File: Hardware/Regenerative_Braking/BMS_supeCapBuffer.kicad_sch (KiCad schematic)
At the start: 0 parts

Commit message: finished with sensing circuits & cap banks
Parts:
- added ACS712-30A3: (no value), Regen_braking:Solderpad_acs712_INOUT, symbol Regen_braking:solder_pad_acs712_inout
- added ACS712-30A4: (no value), Regen_braking:ACS712_Module_27x12mm, symbol Regen_braking:ACS712-30A
- added C21: 4.7uf_50v_VDDcap, Regen_braking:4.7uf_50v_VDDcap, symbol Regen_braking:4.7uf_50v_VDDcap
- added C22: 0.47uf_50v_BScap, Regen_braking:0.47uf_50v_BScap, symbol Regen_braking:0.47uf_50v_BScap
- added C23, C25: 1nf_snubber, Regen_braking:4.7uf_50v_VDDcap, symbol Regen_braking:1nf_snubber
- added C26, C27, C28, C29, C30, C31: 1000uf, Regen_braking:1000uf, symbol Regen_braking:1000uf
- added C_Hi, C_Li: 33p, Regen_braking:33pf_ChiCli, symbol Regen_braking:33pf_ChiCli
- added D11: D_boot, Regen_braking:boot_diode, symbol Regen_braking:D_boot
- added D12: SS34_H, Regen_braking:DIO_SS34, symbol Regen_braking:SS34_BootDiode
- added D13: SS34_L, Regen_braking:DIO_SS34, symbol Regen_braking:SS34_BootDiode
- added IC5: UCC27710DR, Regen_braking:UCC27710DR, symbol Regen_braking:UCC27710DR
- added L2: 33uh, Regen_braking:L_bdc, symbol Device:L
- added Q7, Q8: (no value), Regen_braking:IRLR3705ZPBF, symbol Regen_braking:IRLR3705ZPBF
- added R23, R24: 22ohm_snubber, Regen_braking:Rboot_22ohm, symbol Regen_braking:22ohm_snubber
- added R_Hi, R_Li: 47, Regen_braking:47,2.2,100k,10k,4.7,10ohm, symbol Regen_braking:47,2.2,100k,10k,4.7,10ohm
- added Rboot4: 2.2, Regen_braking:47,2.2,100k,10k,4.7,10ohm, symbol Regen_braking:47,2.2,100k,10k,4.7,10ohm
- added Rgs_H, Rgs_L: 10k, Regen_braking:47,2.2,100k,10k,4.7,10ohm, symbol Regen_braking:47,2.2,100k,10k,4.7,10ohm
- added Roff_h, Roff_l: 4.7, Regen_braking:47,2.2,100k,10k,4.7,10ohm, symbol Regen_braking:47,2.2,100k,10k,4.7,10ohm
- added Ron_h, Ron_l: 10, Regen_braking:47,2.2,100k,10k,4.7,10ohm, symbol Regen_braking:47,2.2,100k,10k,4.7,10ohm
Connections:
- new net: D13.C, Roff_l.2
- new net: C23.1, R24.2
- new net: C25.1, R23.2
- new net: D11.2 (A), Rboot4.2
- new net: D12.C, Roff_h.2
- new net 0: ACS712-30A4. (VCC), C21.2, C23.2, C26.N, C27.N, C28.N, C29.N, C30.N, C31.N, C_Hi.2, C_Li.2, IC5.4 (COM), Q8.3 (S), Rgs_L.1
- new net 5V: ACS712-30A4. (VCC)
- new net ACS_in: ACS712-30A3. (OUT), L2.2
- new net Cap_bufferBank: ACS712-30A3. (OUT), C26.P, C27.P, C28.P, C29.P, C30.P, C31.P
- new net GH: D12.A, Q7.1 (G), Rgs_H.2, Ron_h.2
- new net GL: D13.A, Q8.1 (G), Rgs_L.2, Ron_l.2
- new net HIN: C_Hi.1, IC5.2 (HI), R_Hi.2
- new net LIN: C_Li.1, IC5.3 (LI), R_Li.2
- new net QH_in: R_Hi.1
- new net QH_out: IC5.7 (HO), Roff_h.1, Ron_h.1
- new net QL_in: R_Li.1
- new net QL_out: IC5.5 (LO), Roff_l.1, Ron_l.1
- new net VB: C22.1, D11.1 (K), IC5.8 (HB)
- new net VBUS: Q7.2 (D), R23.1
- new net VDD: C21.1, IC5.1 (VDD), Rboot4.1
- new net VS: C22.2, C25.2, IC5.6 (HS), L2.1, Q7.3 (S), Q8.2 (D), R24.1, Rgs_H.1
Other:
- note added: "BIDIRECTIONAL CONVERTER STAGE"
- note added: "CAPACITOR BUFFER BANK"

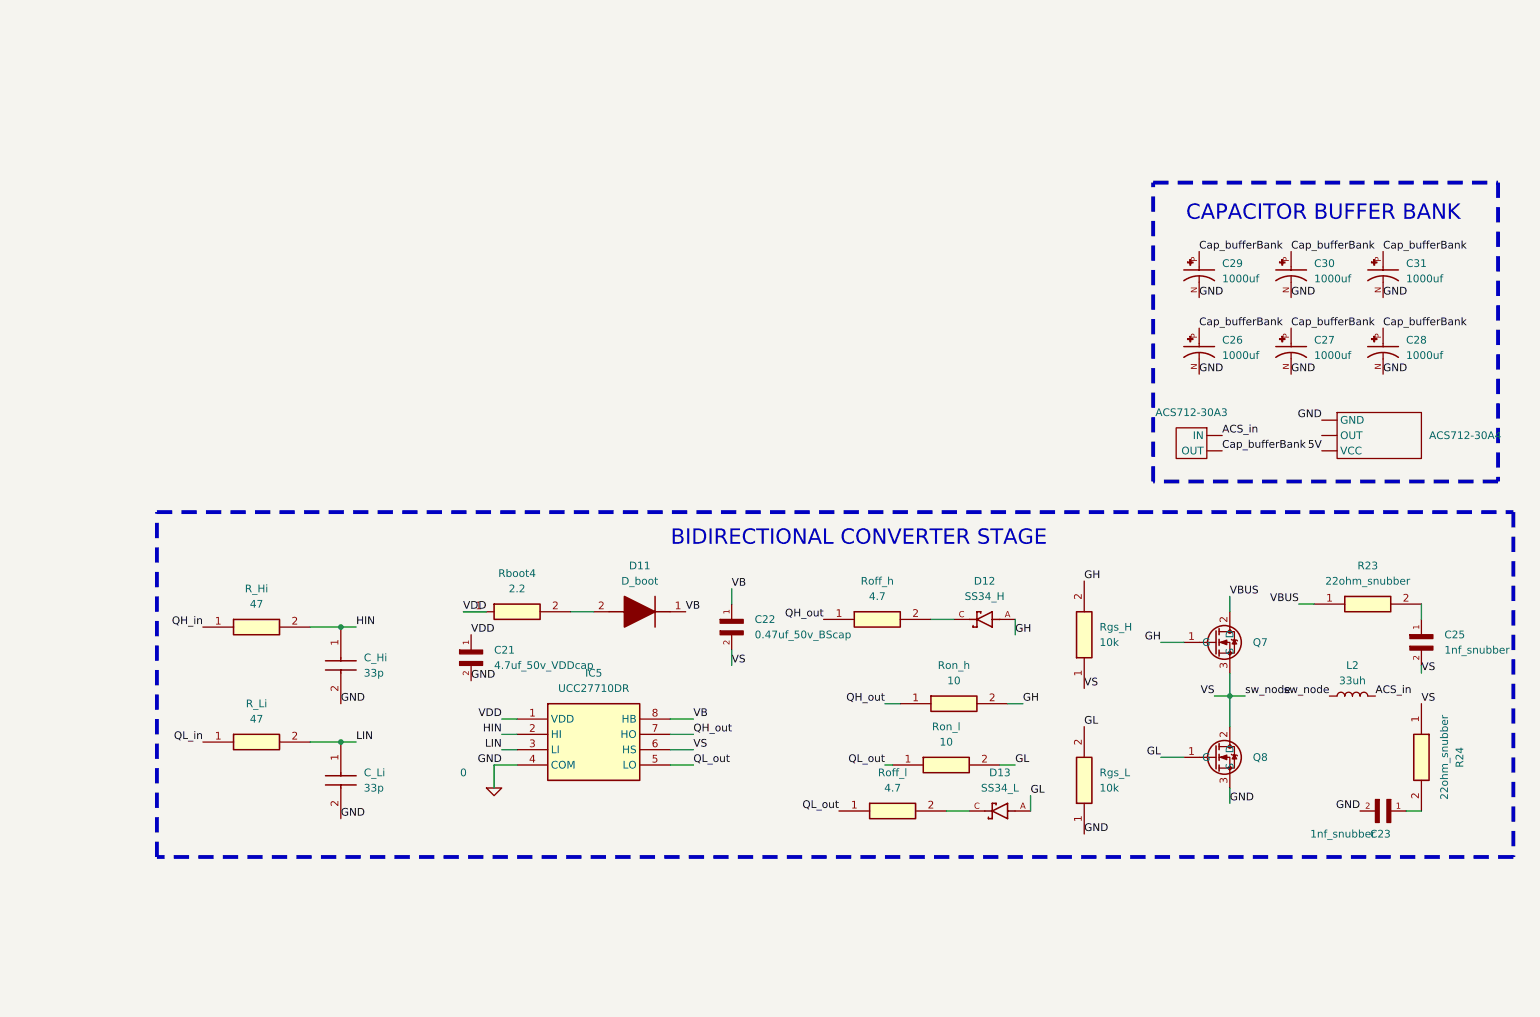
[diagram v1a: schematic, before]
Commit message: Added Battery side
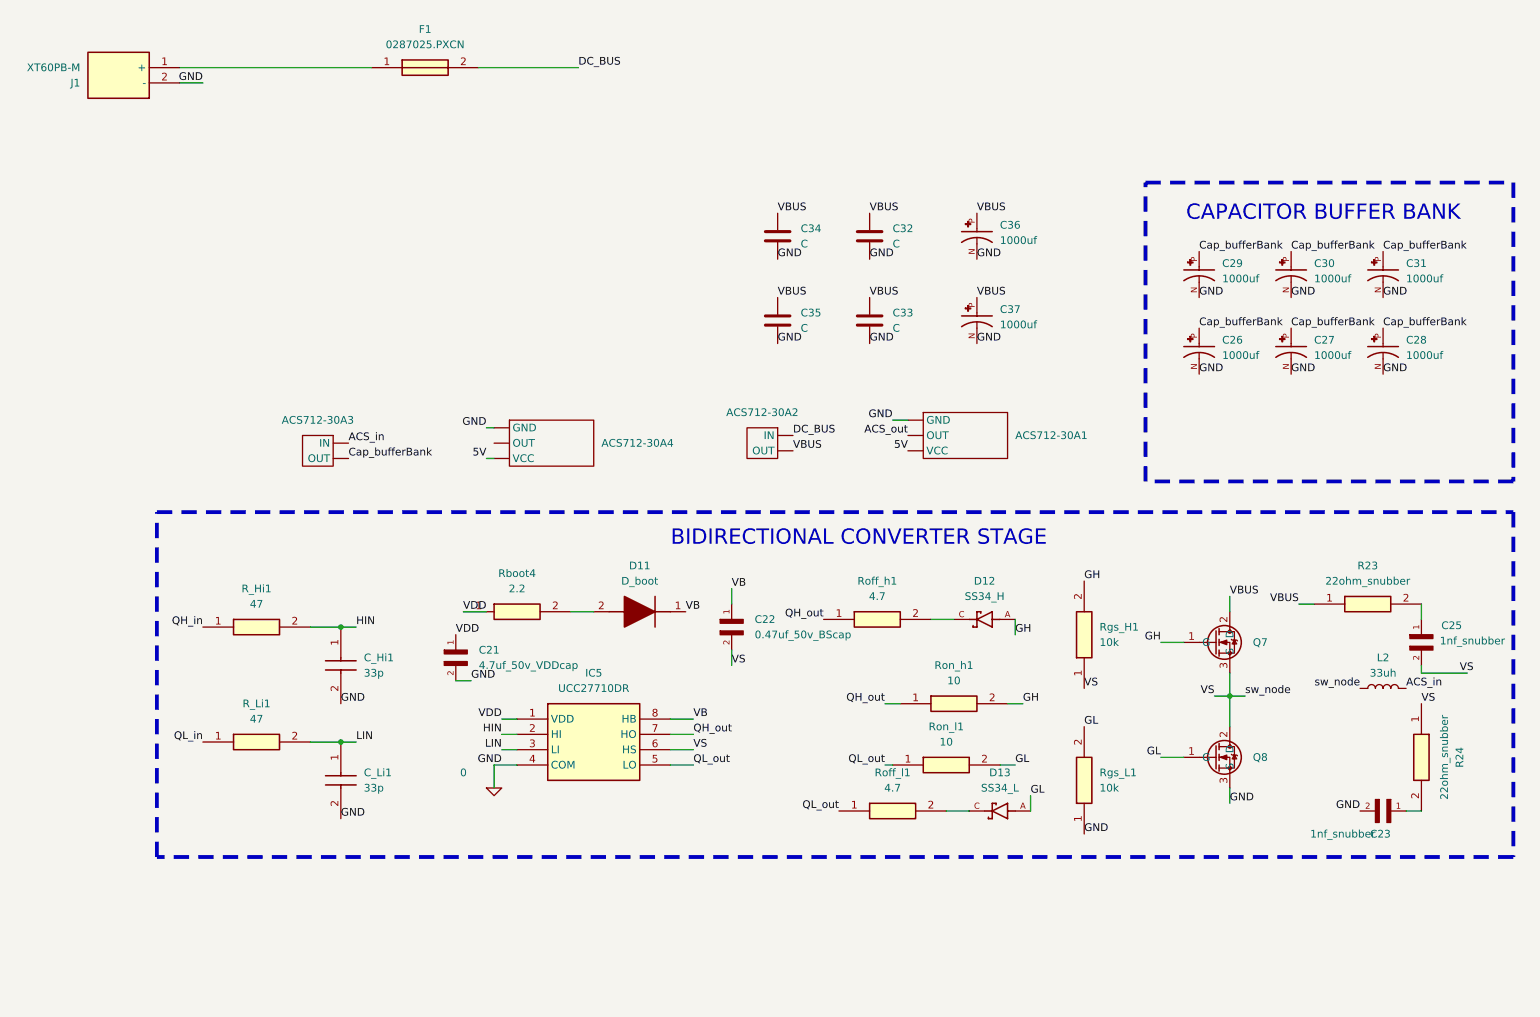
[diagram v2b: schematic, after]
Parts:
- added ACS712-30A1: (no value), Regen_braking:ACS712_Module_27x12mm, symbol Regen_braking:ACS712-30A
- added ACS712-30A2: (no value), Regen_braking:Solderpad_acs712_INOUT, symbol Regen_braking:solder_pad_acs712_inout
- added C32, C33, C34, C35: C, symbol Device:C
- added C36, C37: 1000uf, Regen_braking:1000uf, symbol Regen_braking:1000uf
- added F1: 0287025.PXCN, 0287025PXCN, symbol Regen_braking:0287025.PXCN
- added J1: XT60PB-M, XT60PBM, symbol Regen_braking:XT60PB-M
- renumbered C_Hi to C_Hi1, C_Li to C_Li1, R_Hi to R_Hi1, R_Li to R_Li1, Rgs_H to Rgs_H1, Rgs_L to Rgs_L1, Roff_h to Roff_h1, Roff_l to Roff_l1, Ron_h to Ron_h1, Ron_l to Ron_l1
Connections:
- net 0: now also ACS712-30A1. (VCC), C32.2, C33.2, C34.2, C35.2, C36.N, C37.N, J1.2 (-)
- net 5V: now also ACS712-30A1. (VCC)
- net VBUS: now also ACS712-30A2. (OUT), C32.1, C33.1, C34.1, C35.1, C36.P, C37.P
- new net: F1.1, J1.1 (+)
- new net ACS_out: ACS712-30A1. (VCC)
- new net DC_BUS: ACS712-30A2. (OUT), F1.2
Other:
- moved on the sheet: ACS712-30A3, ACS712-30A4, C21, L2

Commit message: finished everything except mcu
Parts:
- removed ACS712-30A1, ACS712-30A4: (no value), Regen_braking:ACS712_Module_27x12mm, symbol Regen_braking:ACS712-30A
- removed ACS712-30A2, ACS712-30A3: (no value), Regen_braking:Solderpad_acs712_INOUT, symbol Regen_braking:solder_pad_acs712_inout
- removed C36, C37: 1000uf, Regen_braking:1000uf, symbol Regen_braking:1000uf
- added C18: 330uf, Regen_braking:330uf_25v_cap_5v_buck, symbol Regen_braking:330uf_25v_cap_5v_buck
- added C24: 120uf, Regen_braking:120uf_cap_5v_buck, symbol Regen_braking:120uf_cap_5v_buck
- added D10: 1N5822, Regen_braking:1N5822, symbol Regen_braking:1N5822
- added L1: 47uH, Regen_braking:47uh_5v_buck, symbol Regen_braking:47uh_5v_buck
- added VR1: LM2596S-5.0, Regen_braking:5v_buck, symbol Regen_braking:LM2596S-5.0
- F1: footprint 0287025PXCN -> Regen_braking:0287025PXCN
- J1: footprint XT60PBM -> Regen_braking:XT60PBM
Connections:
- net 0: now also C18.2 (-), C24.N, D10.A, VR1.3 (GROUND), VR1.5 (~{ON}/OFF), VR1.6 (GND_TAB)
- net 5V: now also C18.1 (+), L1.2, VR1.4 (FEEDBACK)
- net VBUS: now also C24.P, VR1.1 (VIN)
- new net SW: D10.C, L1.1, VR1.2 (OUTPUT)
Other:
- note added: "5V BUCK STAGE"
- moved on the sheet: C26, C27, C28, C29, C30, C31, C32, C33, C34, C35, F1, J1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

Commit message: MCU CONNECTIONS
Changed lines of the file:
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@@
+	(wire
+		(pts
+			(xy 105.41 135.89) (xy 105.41 132.08)
+		)
+		(stroke
+			(width 0)
+			(type default)
+		)
+	)
 	(wire
 		(pts
@@
 	(wire
 		(pts
-			(xy 105.41 132.08) (xy 107.95 132.08)
+			(xy 105.41 135.89) (xy 104.14 135.89)
 		)
 		(stroke
@@
 	)
 	(label "GND"
-		(at 107.95 132.08 0)
-		(effects
-			(font
+		(at 104.14 135.89 0)
+		(effects
+			(font

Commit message: finished schematic
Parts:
- removed C26, C27, C28, C29, C30, C31: 1000uf, Regen_braking:1000uf, symbol Regen_braking:1000uf
- removed C32, C33, C34, C35: C, symbol Device:C
- removed F1: 0287025.PXCN, Regen_braking:0287025PXCN, symbol Regen_braking:0287025.PXCN
- removed R_Hi1, R_Li1: 47, Regen_braking:47,2.2,100k,10k,4.7,10ohm, symbol Regen_braking:47,2.2,100k,10k,4.7,10ohm
- removed Rboot4: 2.2, Regen_braking:47,2.2,100k,10k,4.7,10ohm, symbol Regen_braking:47,2.2,100k,10k,4.7,10ohm
- removed Rgs_H1, Rgs_L1: 10k, Regen_braking:47,2.2,100k,10k,4.7,10ohm, symbol Regen_braking:47,2.2,100k,10k,4.7,10ohm
- removed Roff_h1, Roff_l1: 4.7, Regen_braking:47,2.2,100k,10k,4.7,10ohm, symbol Regen_braking:47,2.2,100k,10k,4.7,10ohm
- removed Ron_h1, Ron_l1: 10, Regen_braking:47,2.2,100k,10k,4.7,10ohm, symbol Regen_braking:47,2.2,100k,10k,4.7,10ohm
- added 3v3_ldo1: (no value), Regen_braking:AMS1117-3.3_Module_26x12mm, symbol Regen_braking:AMS1117-3v3
- added C32, C33, C34, C35, C46, C47, C48, C49, C50, C51: 1000uf, Capacitor_THT:C_Radial_D12.5mm_H25.0mm_P5.00mm, symbol Regen_braking:1000uf
- added C39: 330u, Capacitor_THT:CP_Radial_D10.0mm_P5.00mm, symbol Device:C
- added D14: SMBJ33A, Regen_braking:DIOM5336X244N, symbol Regen_braking:SMBJ33A
- added D15: SS34, Regen_braking:DIO_SS34, symbol Regen_braking:SS34_BootDiode
- added F1: 4628, Regen_braking:FUSE_4628, symbol Regen_braking:4628
- added R63, R64: 47, Resistor_THT:R_Axial_DIN0207_L6.3mm_D2.5mm_P7.62mm_Horizontal, symbol Regen_braking:47,2.2,100k,10k,4.7,10ohm
- added R65: 2.2, Resistor_THT:R_Axial_DIN0207_L6.3mm_D2.5mm_P7.62mm_Horizontal, symbol Regen_braking:47,2.2,100k,10k,4.7,10ohm
- added R66, R67: 4.7, Resistor_THT:R_Axial_DIN0207_L6.3mm_D2.5mm_P7.62mm_Horizontal, symbol Regen_braking:47,2.2,100k,10k,4.7,10ohm
- added R68, R69: 10, Resistor_THT:R_Axial_DIN0207_L6.3mm_D2.5mm_P7.62mm_Horizontal, symbol Regen_braking:47,2.2,100k,10k,4.7,10ohm
- added R70, R71: 10k, Resistor_THT:R_Axial_DIN0204_L3.6mm_D1.6mm_P7.62mm_Horizontal, symbol Regen_braking:47,2.2,100k,10k,4.7,10ohm
- C23, C25: footprint Regen_braking:4.7uf_50v_VDDcap -> Capacitor_SMD:C_1206_3216Metric
- D10: footprint Regen_braking:1N5822 -> Regen_braking:DIOAD1990W125L900D530
- L1: footprint Regen_braking:47uh_5v_buck -> Regen_braking:CDRH8D43NP220NC
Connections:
- net 0: now also C25.2, 3v3_ldo1.2 (GND), 3v3_ldo1.3 (GND), C32.N, C33.N, C34.N, C35.N, C39.2, C46.N, C47.N, C48.N, C49.N, C50.N, C51.N, D14.2 (A), R71.2; no longer C23.2
- net 5V: now also 3v3_ldo1.1 (VIN)
- net Cap_bufferBank: now also C32.P, C33.P, C34.P, C35.P, C46.P, C47.P, C48.P, C49.P, C50.P, C51.P
- net DC_BUS: now also D15.C
- net GH: now also R68.2, R70.1
- net GL: now also R69.2, R71.1
- net HIN: now also R63.2
- net LIN: now also R64.2
- net QH_in: now also R63.1
- net QH_out: now also R66.1, R68.1
- net QL_in: now also R64.1
- net QL_out: now also R67.1, R69.1
- net VDD: now also R65.1
- net VS: now also C23.2, R70.2; no longer C25.2
- net at D13.C: now also R67.2
- net at R24.2: now also C25.1; no longer C23.1
- net at R23.2: now also C23.1; no longer C25.1
- net at D11.2 (A): now also R65.2
- net at D12.C: now also R66.2
- net at J1.1 (+): now also F1.1
- new net: C39.1, D14.1 (K), D15.A, F1.2
- new net 3V3: 3v3_ldo1.4 (VOUT)
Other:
- note added: "3V3 LDO STAGE"
- note added: "BATTERY STAGE"
- moved on the sheet: C18, C24, D10, J1, L1, VR1

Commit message: finished placement
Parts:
- removed 3v3_ldo1: (no value), Regen_braking:AMS1117-3.3_Module_26x12mm, symbol Regen_braking:AMS1117-3v3
- removed C33, C34, C35, C46, C47, C48, C49, C50, C51: 1000uf, Capacitor_THT:C_Radial_D12.5mm_H25.0mm_P5.00mm, symbol Regen_braking:1000uf
- added C10, C11, C12, C13, C14, C5, C6, C7, C8: 1000uf, Capacitor_THT:C_Radial_D12.5mm_H25.0mm_P5.00mm, symbol Regen_braking:1000uf
- added C2: 1u, Capacitor_SMD:C_0805_2012Metric, symbol Device:C
- added J2: Conn_01x01, Connector_PinHeader_2.54mm:PinHeader_1x01_P2.54mm_Vertical, symbol Connector_Generic:Conn_01x01
- added J3, J4: Conn_01x01, Connector_Wire:SolderWirePad_1x01_SMD_1.5x3mm, symbol Connector_Generic:Conn_01x01
- added KCD3-101N1: (no value), Regen_braking:Switch_Rocker_KCD3-101N, symbol Regen_braking:spst_3p
- added NT1: NetTie_2, NetTie:NetTie-2_SMD_Pad2.0mm, symbol Device:NetTie_2
- added NT2: NetTie_4_Cross, NetTie:NetTie-4_SMD_Pad2.0mm, symbol Device:NetTie_4_Cross
- C_Hi1, C_Li1: footprint Regen_braking:33pf_ChiCli -> Capacitor_SMD:C_0805_2012Metric
- R2: renamed from R23; footprint Regen_braking:Rboot_22ohm -> Resistor_THT:R_Axial_DIN0204_L3.6mm_D1.6mm_P7.62mm_Horizontal
- R5: renamed from R63; footprint Resistor_THT:R_Axial_DIN0207_L6.3mm_D2.5mm_P7.62mm_Horizontal -> Resistor_THT:R_Axial_DIN0204_L3.6mm_D1.6mm_P7.62mm_Horizontal
- R7: renamed from R24; footprint Regen_braking:Rboot_22ohm -> Resistor_THT:R_Axial_DIN0204_L3.6mm_D1.6mm_P7.62mm_Horizontal
- R9: renamed from R64; footprint Resistor_THT:R_Axial_DIN0207_L6.3mm_D2.5mm_P7.62mm_Horizontal -> Resistor_THT:R_Axial_DIN0204_L3.6mm_D1.6mm_P7.62mm_Horizontal
- renumbered C39 to C1, C22 to C15, C23 to C16, C21 to C17, C25 to C18, C24 to C3, C32 to C4, C18 to C9, D15 to D1, D14 to D2, D10 to D3, D11 to D4, D12 to D5, D13 to D6, IC5 to IC1, Q7 to Q1, Q8 to Q2, R70 to R1, R69 to R10, R67 to R11, R65 to R3, R66 to R4, R68 to R6, R71 to R8
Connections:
- net 0: now also C4.2, C10.2, C11.2, C12.2, C13.2, C14.2, C2.2, C5.2, C6.2, C7.2, C8.2, NT1.2; no longer C4.N
- net 5V: now also J2.1 (Pin_1)
- net Cap_bufferBank: now also C4.1, C10.1, C11.1, C12.1, C13.1, C14.1, C5.1, C6.1, C7.1, C8.1; no longer C4.P
- net VBUS: now also J3.1 (Pin_1)
- net VS: now also NT2.1; no longer L2.1, Q1.3 (S), Q2.2 (D)
- net at C1.1, D1.A, D2.1 (K): now also C2.1, KCD3-101N1.2 (Load); no longer F1.2
- net QH_in renamed Q_HIGH
- net QL_in renamed Q_LOW
- new net: J4.1 (Pin_1), L2.1
- new net: NT2.3, Q1.3 (S)
- new net: F1.2, KCD3-101N1.1 (Line)
- new net: NT2.4, Q2.2 (D)
- new net GNDA: NT1.1
- no-connect marks 0 -> 2
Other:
- note removed: "3V3 LDO STAGE"
- moved on the sheet: C1, D1, D2, L2

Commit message: ------------------Project Completed Successfully------------------
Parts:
- removed J3: Conn_01x01, Connector_Wire:SolderWirePad_1x01_SMD_1.5x3mm, symbol Connector_Generic:Conn_01x01
- J2: value Conn_01x01 -> 5V
- J4: value Conn_01x01 -> L_in
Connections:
- net VS: now also NT2.2
- net 0 renamed GND
- no-connect marks 2 -> 1
